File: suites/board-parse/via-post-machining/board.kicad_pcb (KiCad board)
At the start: 2 copper layers, 20 x 20 mm, 0 parts

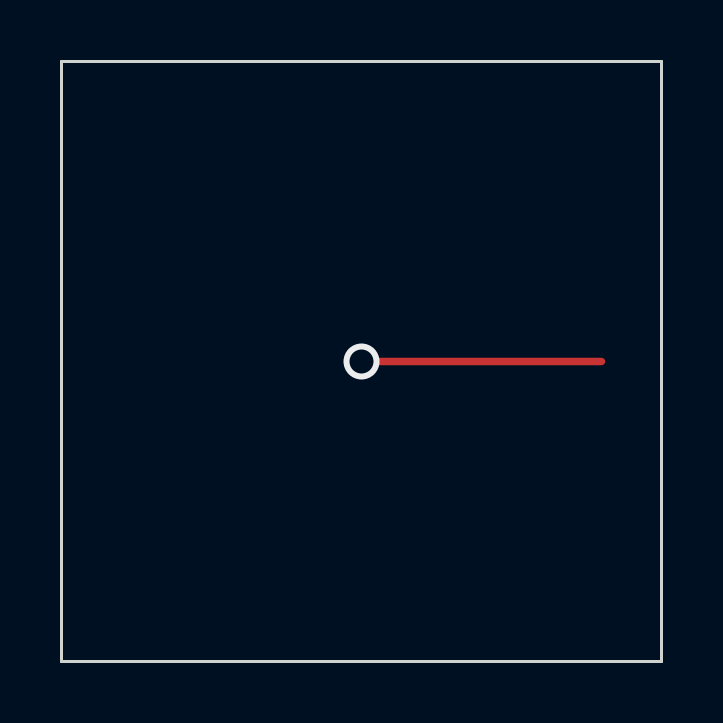
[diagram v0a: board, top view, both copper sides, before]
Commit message: Expand KiCad DRC conformance coverage
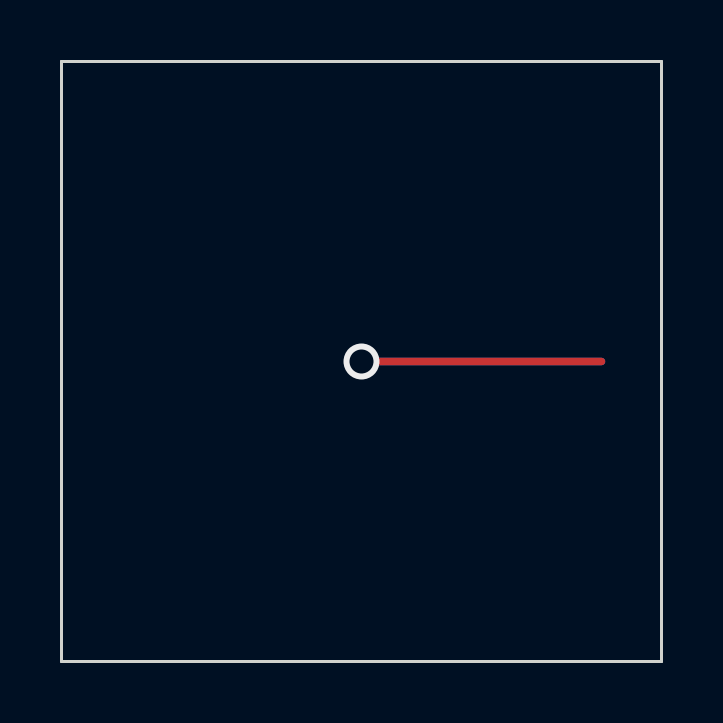
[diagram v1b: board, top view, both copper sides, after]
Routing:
- net Net-1: track 8.00 -> 16.0 mm
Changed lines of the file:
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@@
+		(net "Net-1")
+	)
+	(segment
+		(start 10 10)
+		(end 18 10)
+		(width 0.25)
+		(layer "B.Cu")
 		(net "Net-1")
 	)
